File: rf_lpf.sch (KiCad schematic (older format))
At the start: 7 parts

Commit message: PCB is Done... Needs DRC check
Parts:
- gave numbers to parts that had none: 7
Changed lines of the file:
@@
 $Descr A4 11693 8268
 encoding utf-8
-Sheet 2 14
+Sheet 2 7
 Title "30 MHz Lowpass filter"
 Date "2020 december"
@@
 OUT
 $Comp
-L Device:L L?
+L Device:L L1
 U 1 1 5FE3619B
 P 5100 3400
-F 0 "L?" V 5290 3400 50  0000 C CNN
+F 0 "L1" V 5290 3400 50  0000 C CNN
 F 1 "390n" V 5199 3400 50  0000 C CNN
 F 2 "Inductor_SMD:L_1206_3216Metric_Pad1.42x1.75mm_HandSolder" H 5100 3400 50  0001 C CNN
@@
 $EndComp
 $Comp
-L Device:L L?
+L Device:L L2
 U 1 1 5FE3661E
 P 5900 3400
-F 0 "L?" V 6090 3400 50  0000 C CNN
+F 0 "L2" V 6090 3400 50  0000 C CNN
 F 1 "390n" V 5999 3400 50  0000 C CNN
 F 2 "Inductor_SMD:L_1206_3216Metric_Pad1.42x1.75mm_HandSolder" H 5900 3400 50  0001 C CNN
@@
 $EndComp
 $Comp
-L Device:L L?
+L Device:L L3
 U 1 1 5FE3686B
 P 6700 3400
-F 0 "L?" V 6890 3400 50  0000 C CNN
+F 0 "L3" V 6890 3400 50  0000 C CNN
 F 1 "390n" V 6799 3400 50  0000 C CNN
 F 2 "Inductor_SMD:L_1206_3216Metric_Pad1.42x1.75mm_HandSolder" H 6700 3400 50  0001 C CNN
@@
 $EndComp
 $Comp
-L Device:C C?
+L Device:C C1
 U 1 1 5FE36C7C
 P 4700 3800
-F 0 "C?" H 4815 3846 50  0000 L CNN
+F 0 "C1" H 4815 3846 50  0000 L CNN
 F 1 "150p" H 4815 3755 50  0000 L CNN
 F 2 "Capacitor_SMD:C_0805_2012Metric_Pad1.18x1.45mm_HandSolder" H 4738 3650 50  0001 C CNN
@@
 $EndComp
 $Comp
-L Device:C C?
+L Device:C C4
 U 1 1 5FE36EEB
 P 7100 3800
-F 0 "C?" H 7215 3846 50  0000 L CNN
+F 0 "C4" H 7215 3846 50  0000 L CNN
 F 1 "150p" H 7215 3755 50  0000 L CNN
 F 2 "Capacitor_SMD:C_0805_2012Metric_Pad1.18x1.45mm_HandSolder" H 7138 3650 50  0001 C CNN
@@
 $EndComp
 $Comp
-L Device:C C?
+L Device:C C2
 U 1 1 5FE370C8
 P 5500 3800
-F 0 "C?" H 5615 3846 50  0000 L CNN
+F 0 "C2" H 5615 3846 50  0000 L CNN
 F 1 "270p" H 5615 3755 50  0000 L CNN
 F 2 "Capacitor_SMD:C_0805_2012Metric_Pad1.18x1.45mm_HandSolder" H 5538 3650 50  0001 C CNN
@@
 $EndComp
 $Comp
-L Device:C C?
+L Device:C C3
 U 1 1 5FE373A2
 P 6300 3800
-F 0 "C?" H 6415 3846 50  0000 L CNN
+F 0 "C3" H 6415 3846 50  0000 L CNN
 F 1 "270p" H 6415 3755 50  0000 L CNN
 F 2 "Capacitor_SMD:C_0805_2012Metric_Pad1.18x1.45mm_HandSolder" H 6338 3650 50  0001 C CNN
@@
 	5900 4200 6300 4200
 $Comp
-L power:GNDA #PWR?
+L power:GNDA #PWR01
 U 1 1 5FE4B301
 P 5900 4350
-F 0 "#PWR?" H 5900 4100 50  0001 C CNN
+F 0 "#PWR01" H 5900 4100 50  0001 C CNN
 F 1 "GNDA" H 5905 4177 50  0000 C CNN
 F 2 "" H 5900 4350 50  0001 C CNN

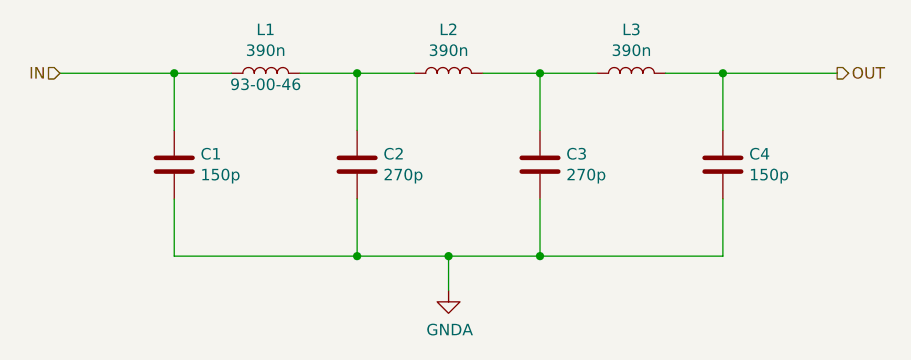
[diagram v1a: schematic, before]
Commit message: RX PCB revision: Diff amp + Mixer2
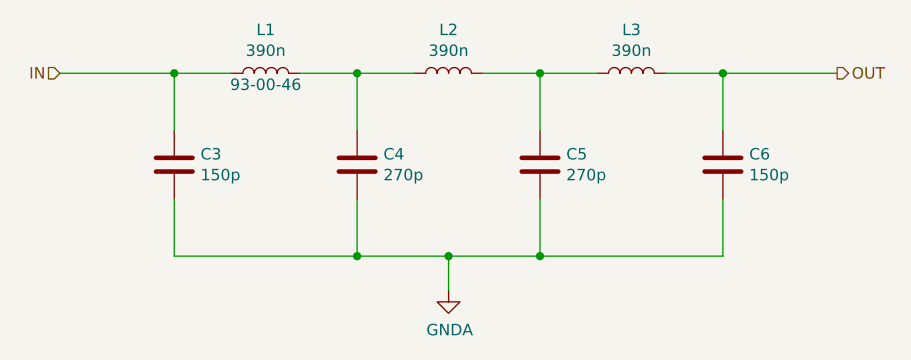
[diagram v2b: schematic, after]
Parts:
- C3: renamed from C1; footprint Capacitor_SMD:C_0805_2012Metric_Pad1.18x1.45mm_HandSolder -> Capacitor_SMD:C_0805_2012Metric_Pad1.15x1.40mm_HandSolder
- C4: renamed from C2; footprint Capacitor_SMD:C_0805_2012Metric_Pad1.18x1.45mm_HandSolder -> Capacitor_SMD:C_0805_2012Metric_Pad1.15x1.40mm_HandSolder
- C5: renamed from C3; footprint Capacitor_SMD:C_0805_2012Metric_Pad1.18x1.45mm_HandSolder -> Capacitor_SMD:C_0805_2012Metric_Pad1.15x1.40mm_HandSolder
- C6: renamed from C4; footprint Capacitor_SMD:C_0805_2012Metric_Pad1.18x1.45mm_HandSolder -> Capacitor_SMD:C_0805_2012Metric_Pad1.15x1.40mm_HandSolder
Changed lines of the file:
@@
 $EndComp
 $Comp
-L Device:C C1
+L Device:C C3
 U 1 1 5FE36C7C
 P 4700 3800
-F 0 "C1" H 4815 3846 50  0000 L CNN
+F 0 "C3" H 4815 3846 50  0000 L CNN
 F 1 "150p" H 4815 3755 50  0000 L CNN
-F 2 "Capacitor_SMD:C_0805_2012Metric_Pad1.18x1.45mm_HandSolder" H 4738 3650 50  0001 C CNN
+F 2 "Capacitor_SMD:C_0805_2012Metric_Pad1.15x1.40mm_HandSolder" H 4738 3650 50  0001 C CNN
 F 3 "~" H 4700 3800 50  0001 C CNN
 	1    4700 3800
@@
 $EndComp
 $Comp
-L Device:C C4
+L Device:C C6
 U 1 1 5FE36EEB
 P 7100 3800
-F 0 "C4" H 7215 3846 50  0000 L CNN
+F 0 "C6" H 7215 3846 50  0000 L CNN
 F 1 "150p" H 7215 3755 50  0000 L CNN
-F 2 "Capacitor_SMD:C_0805_2012Metric_Pad1.18x1.45mm_HandSolder" H 7138 3650 50  0001 C CNN
+F 2 "Capacitor_SMD:C_0805_2012Metric_Pad1.15x1.40mm_HandSolder" H 7138 3650 50  0001 C CNN
 F 3 "~" H 7100 3800 50  0001 C CNN
 	1    7100 3800
@@
 $EndComp
 $Comp
-L Device:C C2
+L Device:C C4
 U 1 1 5FE370C8
 P 5500 3800
-F 0 "C2" H 5615 3846 50  0000 L CNN
+F 0 "C4" H 5615 3846 50  0000 L CNN
 F 1 "270p" H 5615 3755 50  0000 L CNN
-F 2 "Capacitor_SMD:C_0805_2012Metric_Pad1.18x1.45mm_HandSolder" H 5538 3650 50  0001 C CNN
+F 2 "Capacitor_SMD:C_0805_2012Metric_Pad1.15x1.40mm_HandSolder" H 5538 3650 50  0001 C CNN
 F 3 "~" H 5500 3800 50  0001 C CNN
 	1    5500 3800
@@
 $EndComp
 $Comp
-L Device:C C3
+L Device:C C5
 U 1 1 5FE373A2
 P 6300 3800
-F 0 "C3" H 6415 3846 50  0000 L CNN
+F 0 "C5" H 6415 3846 50  0000 L CNN
 F 1 "270p" H 6415 3755 50  0000 L CNN
-F 2 "Capacitor_SMD:C_0805_2012Metric_Pad1.18x1.45mm_HandSolder" H 6338 3650 50  0001 C CNN
+F 2 "Capacitor_SMD:C_0805_2012Metric_Pad1.15x1.40mm_HandSolder" H 6338 3650 50  0001 C CNN
 F 3 "~" H 6300 3800 50  0001 C CNN
 	1    6300 3800
@@
 	5900 4200 6300 4200
 $Comp
-L power:GNDA #PWR01
+L power:GNDA #PWR014
 U 1 1 5FE4B301
 P 5900 4350
-F 0 "#PWR01" H 5900 4100 50  0001 C CNN
+F 0 "#PWR014" H 5900 4100 50  0001 C CNN
 F 1 "GNDA" H 5905 4177 50  0000 C CNN
 F 2 "" H 5900 4350 50  0001 C CNN
